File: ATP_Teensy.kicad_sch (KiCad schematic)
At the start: 7 parts

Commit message: add footprints
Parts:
- removed C? (x2): 10nF, symbol Device:C
- removed IC?: TEENSY_4.1, TEENSY41, symbol ATP_Teensy-lib:TEENSY_4.1
- removed U?: Adafruit_Ultimate_GPS, symbol ATP_Teensy-lib:Adafruit_Ultimate_GPS
- removed U?: BMP388_3966, symbol ATP_Teensy-lib:BMP388_3966
- removed U?: L7805CV, TO-220_STM, symbol ATP_Teensy-lib:L7805CV
- removed U?: MPU6050, symbol ATP_Teensy-lib:MPU6050
- added C1, C2: 10nF, Capacitor_SMD:C_0805_2012Metric_Pad1.18x1.45mm_HandSolder, symbol Device:C_Small
- added J1: Screw_Terminal_01x02, TerminalBlock:TerminalBlock_bornier-2_P5.08mm, symbol Connector:Screw_Terminal_01x02
- added U1: BMP388_3966, Connector_PinSocket_2.54mm:PinSocket_1x08_P2.54mm_Vertical, symbol ATP_Teensy-lib:BMP388_3966
- added U2: L7805CV, ATP_Teensy_footprints:L7805CV, symbol ATP_Teensy-lib:L7805CV
- added U3: MPU6050, ATP_Teensy_footprints:IMU_board, symbol ATP_Teensy-lib:MPU6050
- added U4: Adafruit_Ultimate_GPS, ATP_Teensy_footprints:GPS_board, symbol ATP_Teensy-lib:Adafruit_Ultimate_GPS
- added U5: Teensy4.1, teensy:Teensy41, symbol teensy:Teensy4.1
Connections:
- net +5V: now also C2.2, U1.1 (VIN), U2.3 (OUT), U3.1 (VCC), U4.8 (VIN), U5.48 (VIN)
- net +9V: now also C1.2, J1.1 (Pin_1), U2.1 (IN)
- net BMP_SCK: now also U1.4 (SCK), U5.38 (16_A2_RX4_SCL1)
- net BMP_SDI: now also U1.6 (SDI), U5.39 (17_A3_TX4_SDA1)
- net GND: now also C1.1, C2.1, J1.2 (Pin_2), U1.3 (GND), U2.2 (GND), U3.2 (GND), U4.7 (GND), U5.1 (GND), U5.34 (GND), U5.47 (GND)
- net GPS_RX: now also U4.6 (RX), U5.10 (8_TX2_IN1)
- net GPS_TX: now also U4.5 (TX), U5.9 (7_RX2_OUT1A)
- net MPU_SCL: now also U3.3 (SCL), U5.16 (24_A10_TX6_SCL2)
- net MPU_SDA: now also U3.4 (SDA), U5.17 (25_A11_RX6_SDA2)
- no-connect marks 15 -> 72
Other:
- note added: "Last Modified by: Alexandra Zhang Jiang on OCT 30th, 2022"
- note removed: "Last Modified by: Alexandra Zhang Jiang on OCT 25th, 2022"
- note removed: "Note: - pin 42 does not match pinout - pins 48-71 does not match pinout either - no pin 0"
- note removed: "SCL"
- note removed: "SCL1"
- note removed: "SDA"
- note removed: "SDA1"

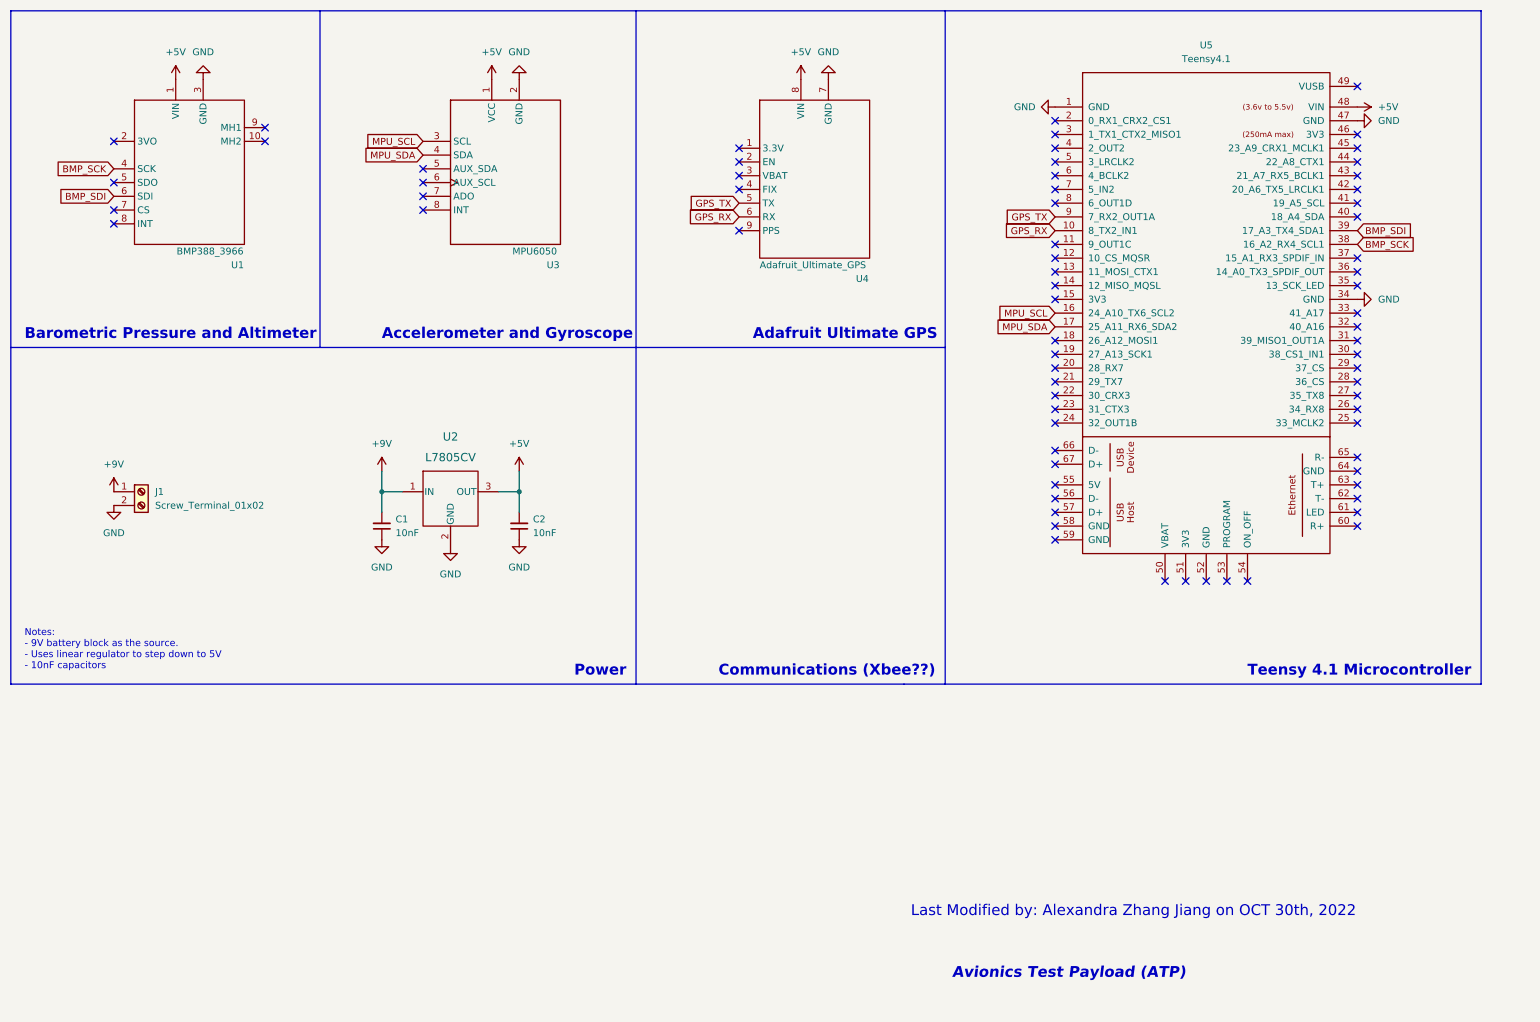
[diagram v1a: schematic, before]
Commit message: Add LED indicators
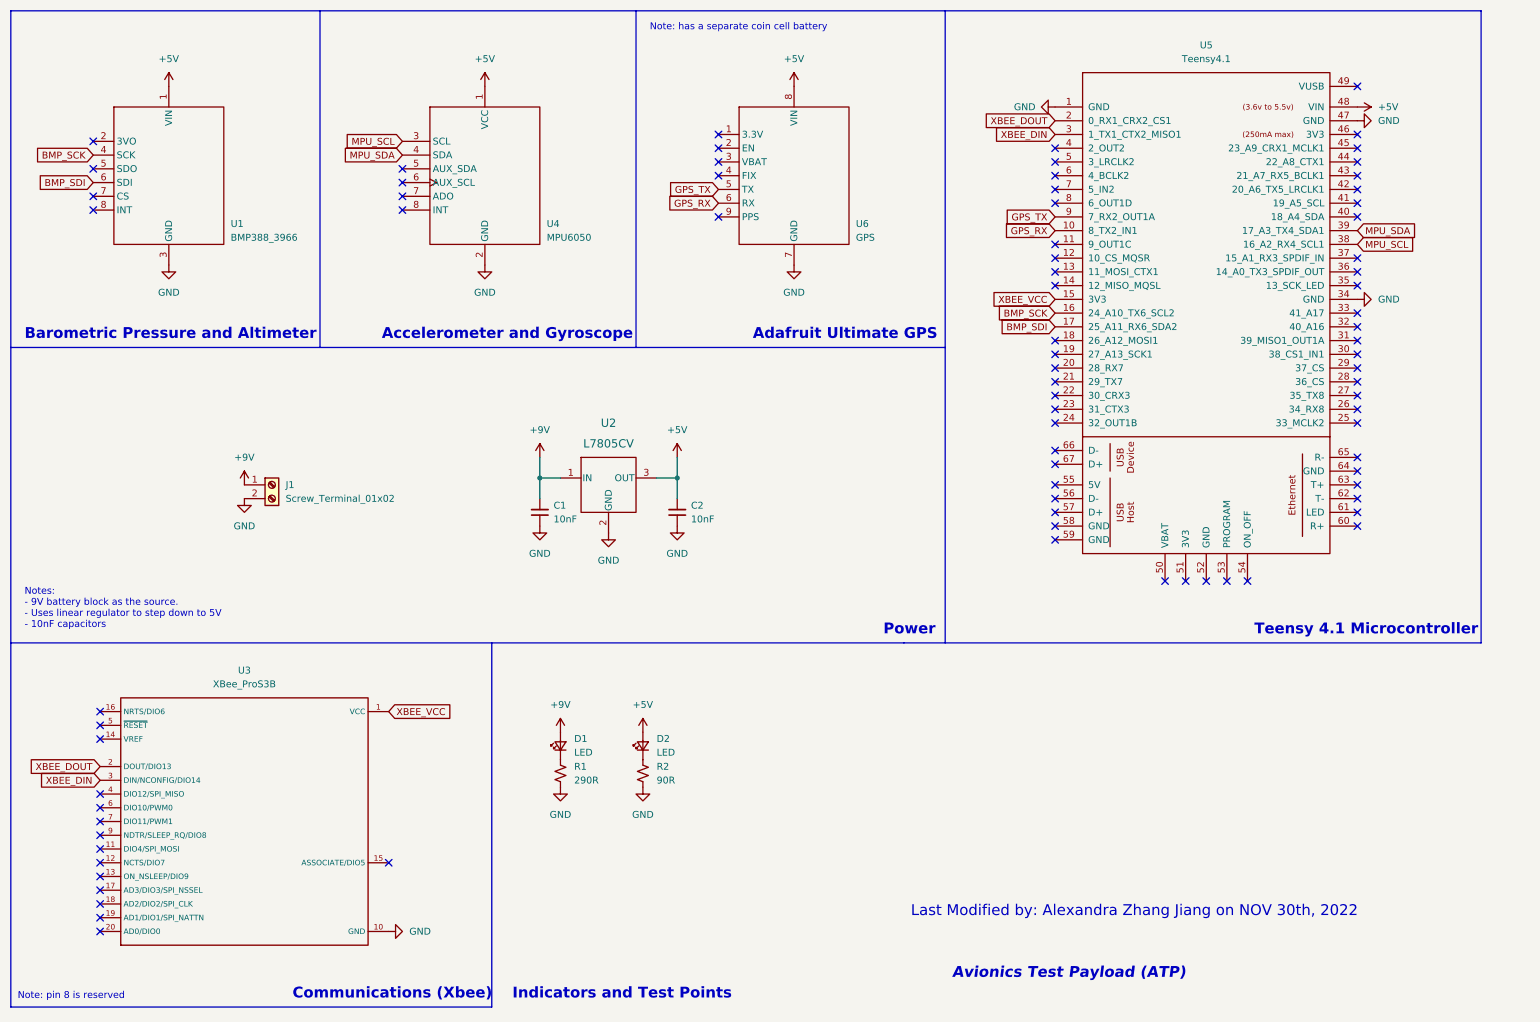
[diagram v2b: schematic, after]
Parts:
- removed U3: MPU6050, ATP_Teensy_footprints:IMU_board, symbol ATP_Teensy-lib:MPU6050
- removed U4: Adafruit_Ultimate_GPS, ATP_Teensy_footprints:GPS_board, symbol ATP_Teensy-lib:Adafruit_Ultimate_GPS
- added D1, D2: LED, LED_SMD:LED_0805_2012Metric_Pad1.15x1.40mm_HandSolder, symbol Device:LED_Small
- added R1: 290R, Resistor_SMD:R_0805_2012Metric_Pad1.20x1.40mm_HandSolder, symbol Device:R_Small_US
- added R2: 90R, Resistor_SMD:R_0805_2012Metric_Pad1.20x1.40mm_HandSolder, symbol Device:R_Small_US
- added U3: XBee_ProS3B, ATP_Teensy_footprints:XBEE_board, symbol ATP_Teensy-lib:XBee_ProS3B
- added U4: MPU6050, ATP_Teensy_footprints:IMU_board, symbol ATP_Teensy-lib:MPU6050
- added U6: GPS, ATP_Teensy_footprints:GPS_board, symbol ATP_Teensy-lib:Adafruit_Ultimate_GPS
- U1: footprint Connector_PinSocket_2.54mm:PinSocket_1x08_P2.54mm_Vertical -> ATP_Teensy_footprints:BMP_board
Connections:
- net +5V: now also D2.2 (A), U4.1 (VCC), U6.8 (VIN)
- net +9V: now also D1.2 (A)
- net BMP_SCK: now also U5.16 (24_A10_TX6_SCL2); no longer U5.38 (16_A2_RX4_SCL1)
- net BMP_SDI: now also U5.17 (25_A11_RX6_SDA2); no longer U5.39 (17_A3_TX4_SDA1)
- net GND: now also R1.2, R2.2, U3.10 (GND), U4.2 (GND), U6.7 (GND)
- net GPS_RX: now also U6.6 (RX)
- net GPS_TX: now also U6.5 (TX)
- net MPU_SCL: now also U5.38 (16_A2_RX4_SCL1), U4.3 (SCL); no longer U5.16 (24_A10_TX6_SCL2)
- net MPU_SDA: now also U5.39 (17_A3_TX4_SDA1), U4.4 (SDA); no longer U5.17 (25_A11_RX6_SDA2)
- net XBEE_VCC: now reaches U5.15 (3V3)
- net XBEE_VCC: now also U3.1 (VCC)
- net XBEE_DOUT: now reaches U5.2 (0_RX1_CRX2_CS1)
- net XBEE_DOUT: now also U3.2 (DOUT/DIO13)
- net XBEE_DIN: now reaches U5.3 (1_TX1_CTX2_MISO1)
- net XBEE_DIN: now also U3.3 (DIN/NCONFIG/DIO14)
- new net: D2.1 (K), R2.1
- new net: D1.1 (K), R1.1
- no-connect marks 72 -> 82
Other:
- note added: "Communications (Xbee)"
- note added: "Indicators and Test Points"
- note added: "Last Modified by: Alexandra Zhang Jiang on NOV 30th, 2022"
- note added: "Note: has a separate coin cell battery"
- note added: "Note: pin 8 is reserved"
- note removed: "Communications (Xbee??)"
- note removed: "Last Modified by: Alexandra Zhang Jiang on OCT 30th, 2022"
- moved on the sheet: C1, C2, J1, U2

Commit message: Change BMP connection from I2C to SPI
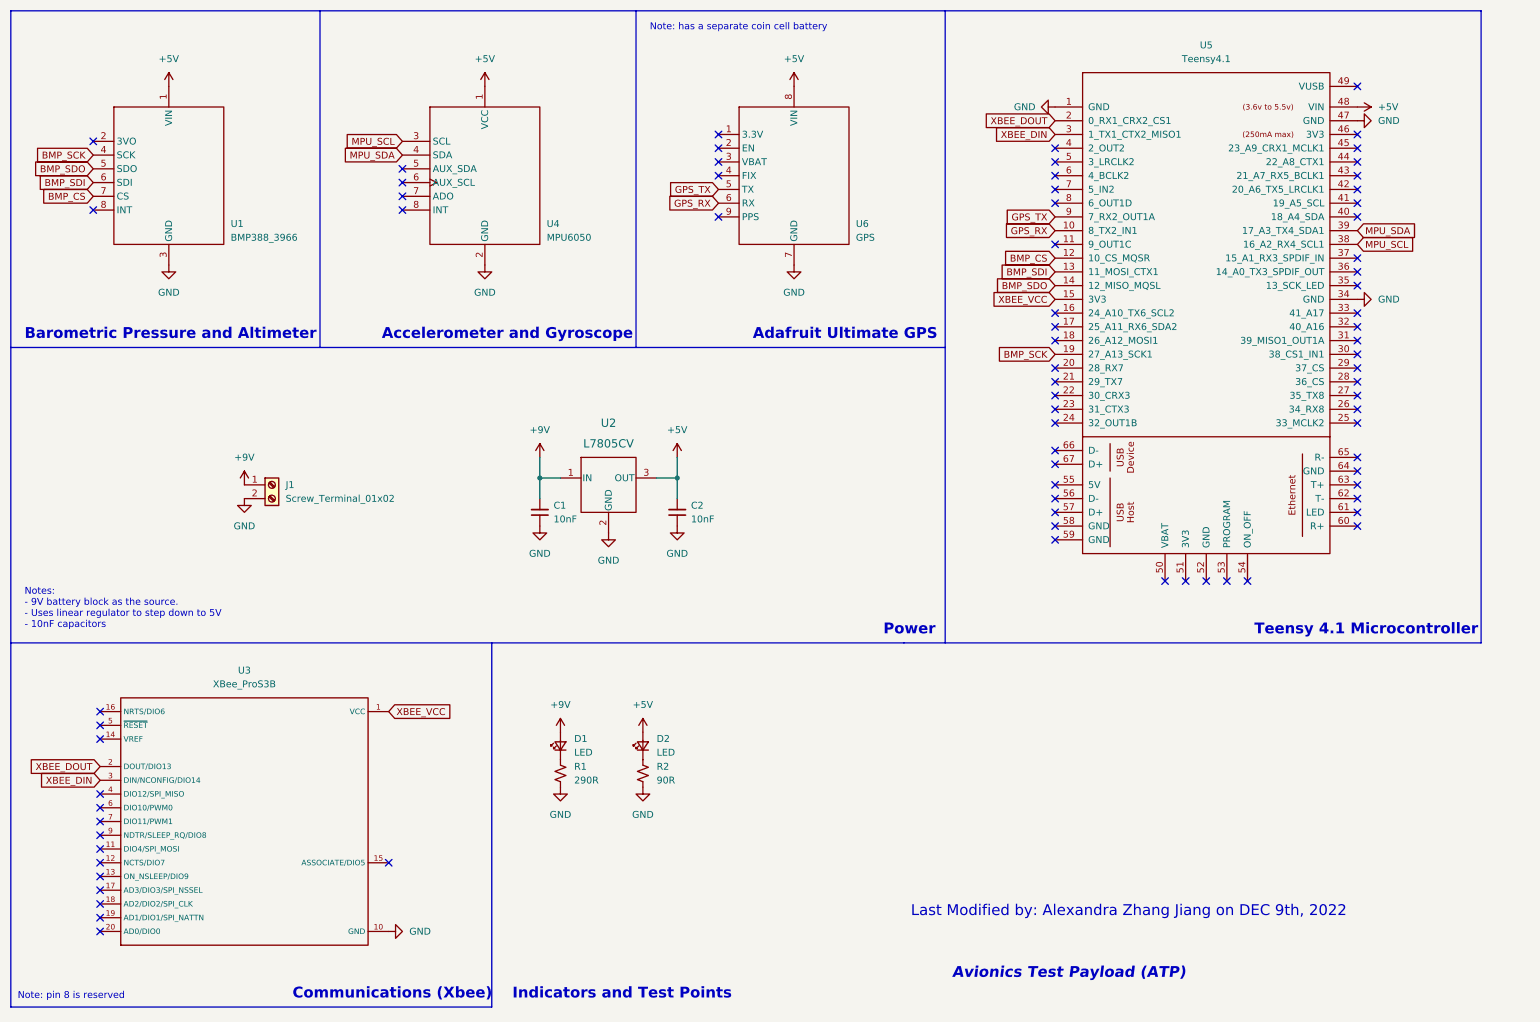
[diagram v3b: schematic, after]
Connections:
- net BMP_SCK: now also U5.19 (27_A13_SCK1); no longer U5.16 (24_A10_TX6_SCL2)
- net BMP_SDI: now also U5.13 (11_MOSI_CTX1); no longer U5.17 (25_A11_RX6_SDA2)
- net BMP_SDO: now reaches U1.5 (SDO)
- net BMP_SDO: now also U5.14 (12_MISO_MQSL)
- net BMP_CS: now reaches U1.7 (CS)
- net BMP_CS: now also U5.12 (10_CS_MQSR)
- no-connect marks 82 -> 78
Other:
- note added: "Last Modified by: Alexandra Zhang Jiang on DEC 9th, 2022"
- note removed: "Last Modified by: Alexandra Zhang Jiang on NOV 30th, 2022"
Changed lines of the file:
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@@
   (no_connect (at 205.74 38.1))
   (no_connect (at 205.74 40.64))
-  (no_connect (at 205.74 63.5))
-  (no_connect (at 205.74 60.96))
   (no_connect (at 205.74 83.82))
   (no_connect (at 205.74 88.9))
@@
   (no_connect (at 205.74 86.36))
   (no_connect (at 205.74 78.74))
-  (no_connect (at 205.74 76.2))
-  (no_connect (at 205.74 58.42))
   (no_connect (at 205.74 55.88))
   (no_connect (at 205.74 73.66))
@@
   (no_connect (at 205.74 100.33))
   (no_connect (at 143.51 43.18))
+  (no_connect (at 205.74 68.58))
+  (no_connect (at 205.74 71.12))
   (no_connect (at 143.51 50.8))
-  (no_connect (at 27.94 41.91))
-  (no_connect (at 27.94 46.99))
   (no_connect (at 27.94 36.83))
   (no_connect (at 143.51 38.1))
@@
     (effects (font (size 2 2) (thickness 0.4) bold) (justify left bottom))
   )
-  (text "Last Modified by: Alexandra Zhang Jiang on NOV 30th, 2022 "
+  (text "Last Modified by: Alexandra Zhang Jiang on DEC 9th, 2022"
     (at 179.07 180.34 0)
     (effects (font (size 2 2)) (justify left bottom))
@@
     (at 15.24 127 0)
     (effects (font (size 1.27 1.27)) (justify left bottom))
+  )
+  (global_label "BMP_CS" (shape input) (at 205.74 58.42 180) (fields_autoplaced)
+    (effects (font (size 1.27 1.27)) (justify right))
+    (property "Intersheet References" "${INTERSHEET_REFS}" (id 0) (at 195.8883 58.3406 0)
+      (effects (font (size 1.27 1.27)) (justify right) hide)
+    )
   )
   (global_label "GPS_RX" (shape input) (at 143.51 48.26 180) (fields_autoplaced)
@@
     )
   )
+  (global_label "BMP_SDO" (shape input) (at 27.94 41.91 180) (fields_autoplaced)
+    (effects (font (size 1.27 1.27)) (justify right))
+    (property "Intersheet References" "${INTERSHEET_REFS}" (id 0) (at 16.7579 41.8306 0)
+      (effects (font (size 1.27 1.27)) (justify right) hide)
+    )
+  )
   (global_label "GPS_RX" (shape input) (at 205.74 53.34 180) (fields_autoplaced)
     (effects (font (size 1.27 1.27)) (justify right))
@@
     )
   )
-  (global_label "BMP_SCK" (shape input) (at 205.74 68.58 180) (fields_autoplaced)
-    (effects (font (size 1.27 1.27)) (justify right))
-    (property "Intersheet References" "${INTERSHEET_REFS}" (id 0) (at 194.6183 68.5006 0)
+  (global_label "BMP_SCK" (shape input) (at 205.74 76.2 180) (fields_autoplaced)
+    (effects (font (size 1.27 1.27)) (justify right))
+    (property "Intersheet References" "${INTERSHEET_REFS}" (id 0) (at 194.6183 76.1206 0)
       (effects (font (size 1.27 1.27)) (justify right) hide)
     )
@@
     )
   )
-  (global_label "BMP_SDI" (shape input) (at 205.74 71.12 180) (fields_autoplaced)
-    (effects (font (size 1.27 1.27)) (justify right))
-    (property "Intersheet References" "${INTERSHEET_REFS}" (id 0) (at 195.2836 71.0406 0)
+  (global_label "BMP_CS" (shape input) (at 27.94 46.99 180) (fields_autoplaced)
+    (effects (font (size 1.27 1.27)) (justify right))
+    (property "Intersheet References" "${INTERSHEET_REFS}" (id 0) (at 18.0883 46.9106 0)
+      (effects (font (size 1.27 1.27)) (justify right) hide)
+    )
+  )
+  (global_label "BMP_SDI" (shape input) (at 205.74 60.96 180) (fields_autoplaced)
+    (effects (font (size 1.27 1.27)) (justify right))
+    (property "Intersheet References" "${INTERSHEET_REFS}" (id 0) (at 195.2836 60.8806 0)
       (effects (font (size 1.27 1.27)) (justify right) hide)
     )
@@
       (effects (font (size 1.27 1.27)) (justify right) hide)
     )
+  )
+  (global_label "BMP_SDO" (shape input) (at 205.74 63.5 180) (fields_autoplaced)
+    (effects (font (size 1.27 1.27)) (justify right))
+    (property "Intersheet References" "${INTERSHEET_REFS}" (id 0) (at 194.5579 63.4206 0)
+      (effects (font (size 1.27 1.27)) (justify right) hide)
+    )

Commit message: Add filtering capacitors for XBee
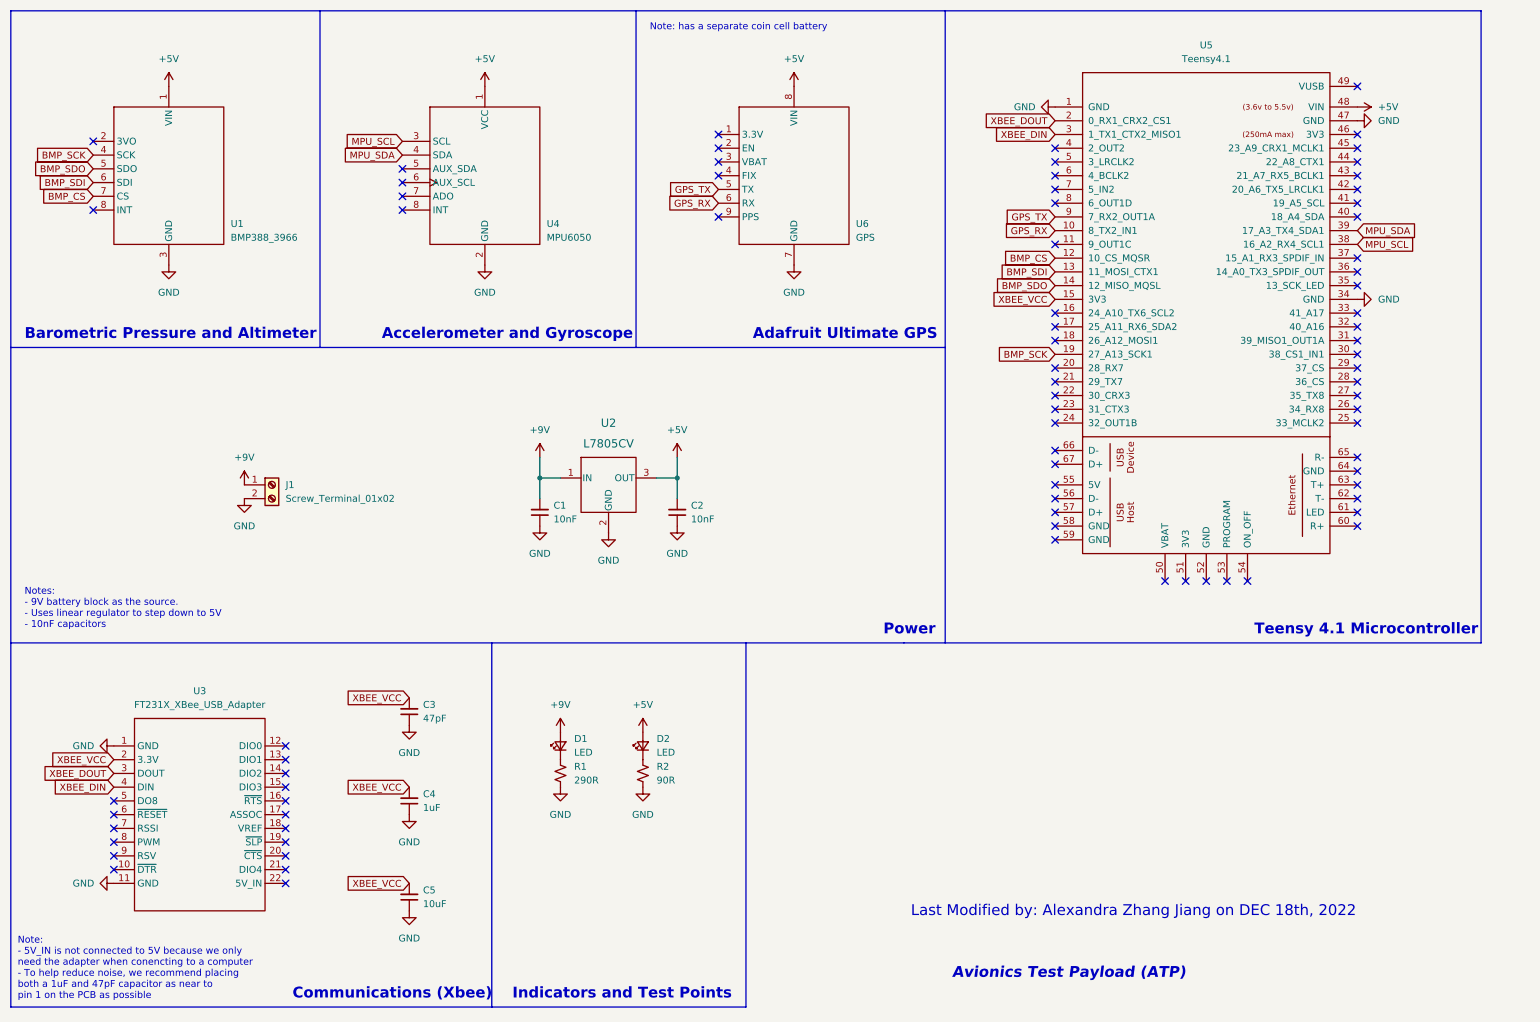
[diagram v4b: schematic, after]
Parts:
- removed U3: XBee_ProS3B, ATP_Teensy_footprints:XBEE_board, symbol ATP_Teensy-lib:XBee_ProS3B
- added C3: 47pF, Capacitor_SMD:C_0805_2012Metric_Pad1.18x1.45mm_HandSolder, symbol Device:C_Small
- added C4: 1uF, Capacitor_SMD:C_0805_2012Metric_Pad1.18x1.45mm_HandSolder, symbol Device:C_Small
- added C5: 10uF, Capacitor_SMD:C_0805_2012Metric_Pad1.18x1.45mm_HandSolder, symbol Device:C_Small
- added U3: FT231X_XBee_USB_Adapter, ATP_Teensy_footprints:XBee_Adapter, symbol ATP_Teensy-lib:FT231X_XBee_USB_Adapter
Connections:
- net GND: now also C3.1, C4.1, C5.1, U3.1 (GND), U3.11 (GND)
- net XBEE_DIN: now also U3.4 (DIN)
- net XBEE_DOUT: now also U3.3 (DOUT)
- net XBEE_VCC: now also C3.2, C4.2, C5.2, U3.2 (3.3V)
- no-connect marks 78 -> 80
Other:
- note added: "Last Modified by: Alexandra Zhang Jiang on DEC 18th, 2022"
- note added: "Note: - 5V_IN is not connected to 5V because we only need the adapter when conencting to a computer - To help reduce noise, we recommend placing both a 1uF and 47pF capacitor as near to pin 1 on the PCB as possible"
- note removed: "Last Modified by: Alexandra Zhang Jiang on DEC 9th, 2022"
- note removed: "Note: pin 8 is reserved"
